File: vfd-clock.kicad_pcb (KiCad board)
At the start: 2 copper layers, 139.7 x 49.5 mm, 24 parts, among them CON1 BARREL_JACK_2, P1 ST_LINK, U1 Maple_Mini_(BTE14-07), U2 CD4056, U3 CD4056, U4 CD4056, U5 CD4056, U6 CD4056, U7 CD4056, U9 MC34063

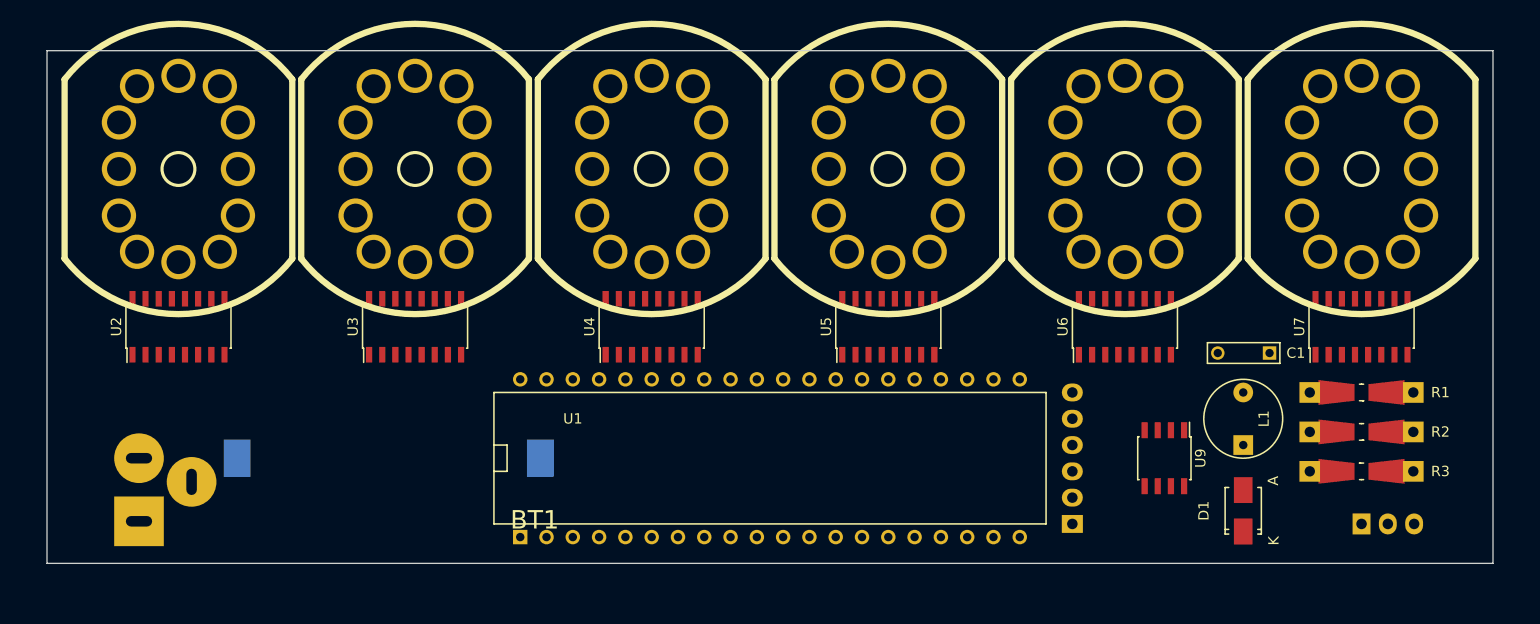
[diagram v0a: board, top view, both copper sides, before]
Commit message: tubes, data bus: routed
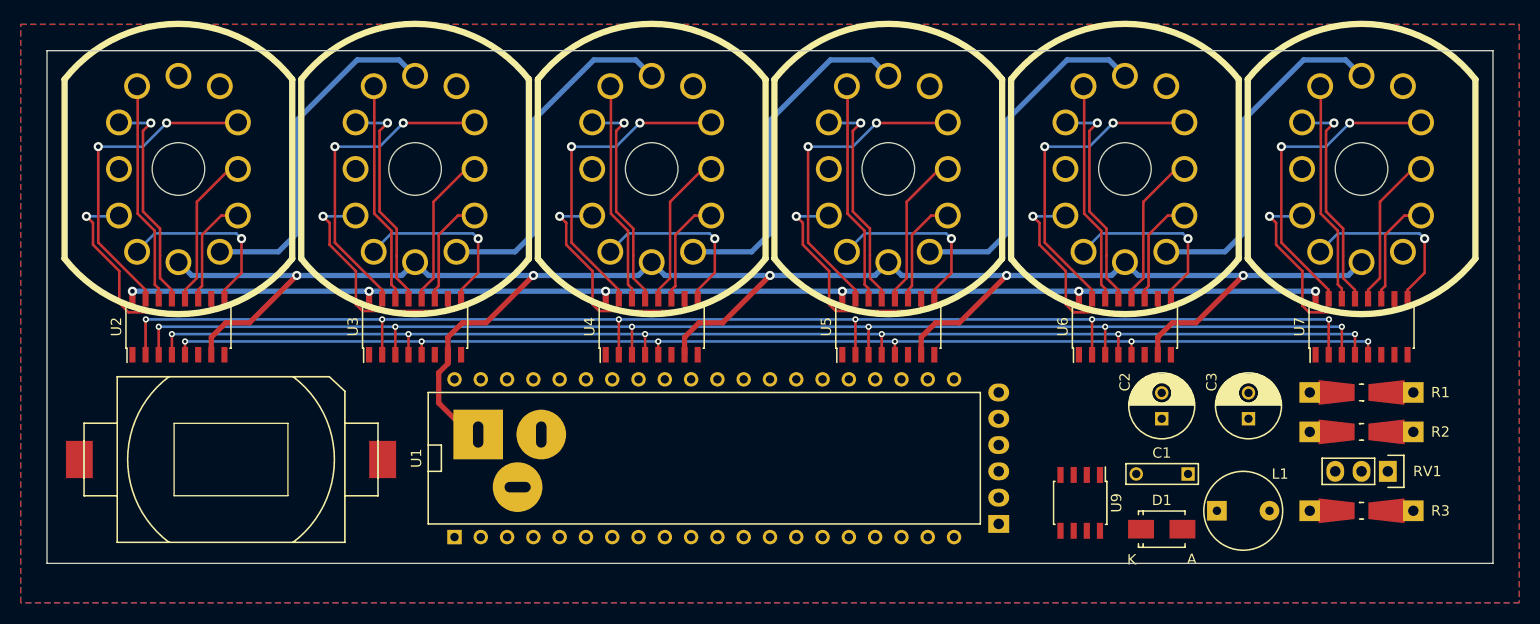
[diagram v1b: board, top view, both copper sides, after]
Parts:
- added C2: 100u, Capacitors_ThroughHole:C_Radial_D6.3_L11.2_P2.5, F.Cu at (122.9, 50.8)
- added C3: 100u, Capacitors_ThroughHole:C_Radial_D6.3_L11.2_P2.5, F.Cu at (131.3, 50.8)
- BT1, RV1: moved to F.Cu
- moved CON1 38.9 mm to (63.0, 52.3), turned to 180 degrees
- moved BT1 15.2 mm to (33.0, 54.7)
- moved C1 14.1 mm to (125.5, 56.1)
- moved U9 9.20 mm to (115.1, 58.9)
- moved L1 8.89 mm to (130.8, 59.7), turned to 0 degrees
- moved D1 8.07 mm to (122.9, 61.5), turned to 0 degrees
- moved P1 7.11 mm to (107.2, 61.0)
- moved U1 6.35 mm to (78.7, 54.6)
- moved RV1 5.68 mm to (144.8, 55.9)
- moved R3 3.81 mm to (142.2, 59.7)
- turned R2 to 0 degrees
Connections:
- net Net-(R1-Pad2) renamed /REG_HI
- V1 pad 12: /7v2 -> /GND
- V1 pad 5: Net-(V1-Pad5) -> /FIL1
- V2 pad 12: Net-(V2-Pad12) -> /FIL1
- V2 pad 5: Net-(V2-Pad5) -> /FIL2
- V3 pad 12: Net-(V3-Pad12) -> /FIL2
- V3 pad 5: Net-(V3-Pad5) -> /FIL3
- V4 pad 12: Net-(V1-Pad5) -> /FIL3
- V4 pad 5: Net-(V2-Pad12) -> /FIL4
- V5 pad 12: Net-(V2-Pad5) -> /FIL4
- V5 pad 5: Net-(V3-Pad12) -> /FIL5
- V6 pad 12: Net-(V3-Pad5) -> /FIL5
- V6 pad 5: /GND -> /7v2
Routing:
- net /19v5: track 0.00 -> 191.9 mm, vias 0 -> 5
- net /DC: track 0.00 -> 134.8 mm, vias 0 -> 6
- net /DB: track 0.00 -> 130.5 mm, vias 0 -> 6
- net /DD: track 0.00 -> 126.2 mm, vias 0 -> 6
- net /DA: track 0.00 -> 122.0 mm, vias 0 -> 6
- net /3v3: track 0.00 -> 118.7 mm, vias 0 -> 6
- net /FIL5: track 0.00 -> 33.6 mm
- net /FIL4: track 0.00 -> 33.6 mm
- net /FIL3: track 0.00 -> 33.6 mm
- net /FIL2: track 0.00 -> 33.6 mm
- net /FIL1: track 0.00 -> 33.6 mm
- net Net-(U6-Pad15): track 0.00 -> 31.1 mm, vias 0 -> 2
- net Net-(U5-Pad15): track 0.00 -> 31.1 mm, vias 0 -> 2
- net Net-(U3-Pad15): track 0.00 -> 31.1 mm, vias 0 -> 2
- net Net-(U7-Pad15): track 0.00 -> 31.1 mm, vias 0 -> 2
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- added copper zone on B.Cu, net /GND
- added copper zone on F.Cu, net /GND
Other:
- net class D_BUS added: clearance 0.254, trace_width 0.254, via_dia 0.6, via_drill 0.3
- net class Power: trace_width 0.381 -> 0.508
- rule via_min_drill: 0.508 -> 0.254
- rule via_min_size: 0.889 -> 0.381

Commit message: first fully routed revision
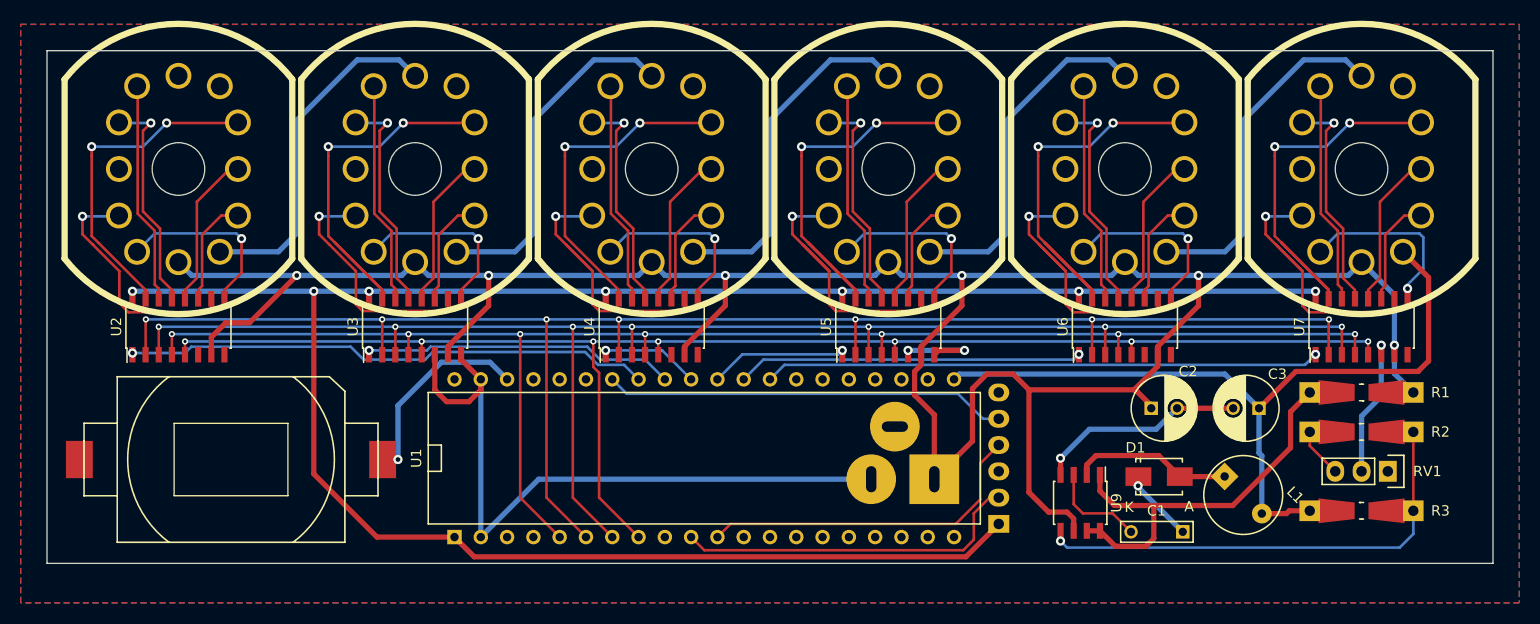
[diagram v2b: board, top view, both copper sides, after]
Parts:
- moved CON1 32.2 mm to (94.9, 56.6), turned to 0 degrees
- moved C1 5.61 mm to (125.0, 61.7)
- moved D1 5.09 mm to (122.7, 56.4)
- moved L1 1.52 mm to (130.8, 58.2), turned to 315 degrees
- moved C2 1.44 mm to (121.9, 49.8), turned to 0 degrees
- moved C3 1.44 mm to (132.3, 49.8), turned to 180 degrees
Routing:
- net /GND: track 0.00 -> 118.5 mm, vias 0 -> 5
- net /3v3: track 118.7 -> 207.1 mm, vias 6 -> 7
- net /7v2: track 0.00 -> 78.5 mm
- net /19v5: track 191.9 -> 250.9 mm, vias 5 -> 6
- net /STROBE6: track 0.00 -> 53.7 mm, vias 0 -> 1
- net /STROBE1: track 0.00 -> 51.2 mm, vias 0 -> 1
- net Net-(R2-Pad2): track 0.00 -> 50.9 mm, vias 0 -> 1
- net /REG_HI: track 0.00 -> 42.1 mm
- net /RST: track 0.00 -> 39.1 mm
- net /SWCLK: track 0.00 -> 33.8 mm
- net /STROBE5: track 0.00 -> 33.4 mm, vias 0 -> 1
- net Net-(U5-Pad15): track 31.1 -> 64.3 mm
- net /SWDIO: track 0.00 -> 32.9 mm
- net /STROBE2: track 0.00 -> 30.5 mm, vias 0 -> 1
- net /DC: track 134.8 -> 157.4 mm, vias 6 -> 7
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
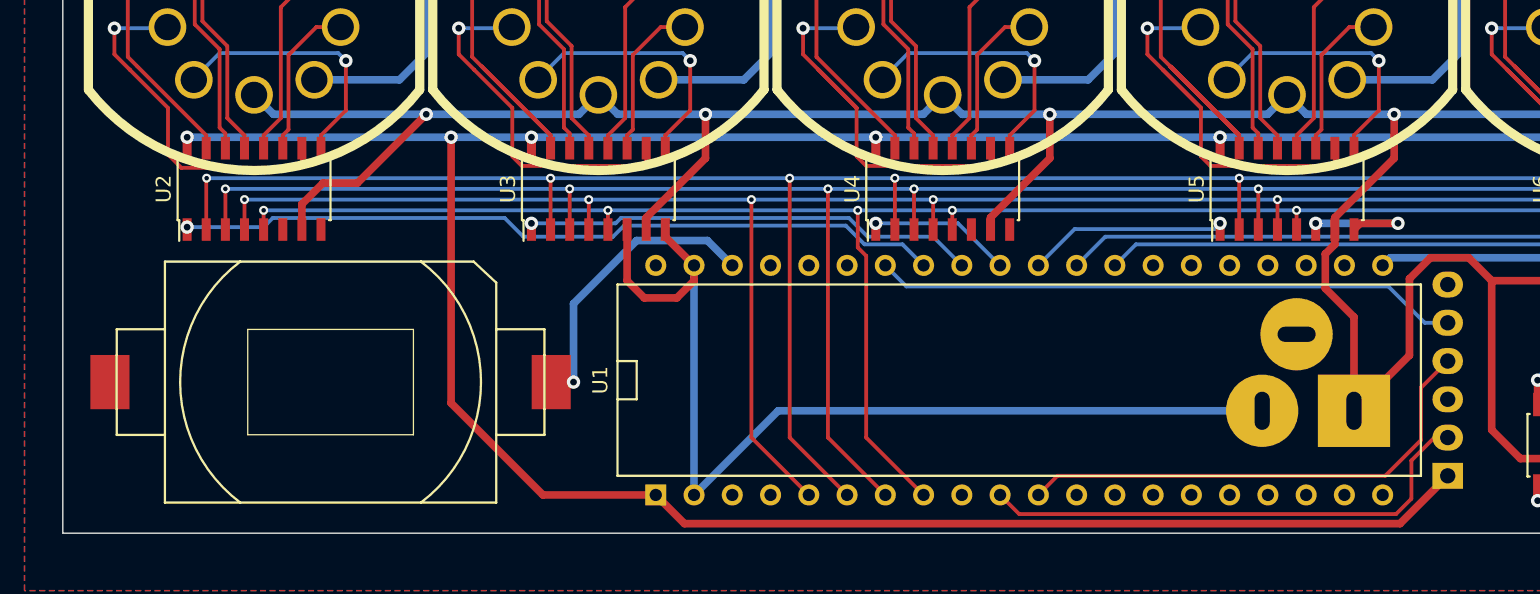
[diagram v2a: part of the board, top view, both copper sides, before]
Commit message: second redundant power connector footprint
(I expect to only ever populate one or the other.)
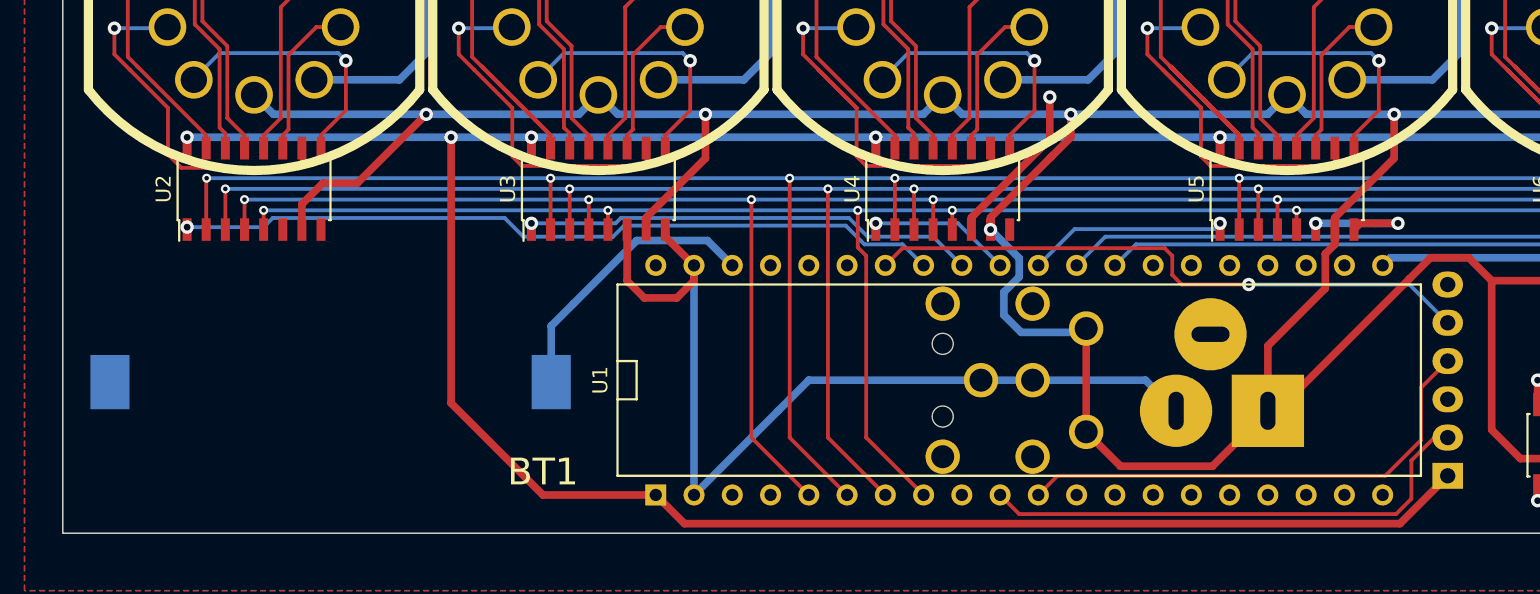
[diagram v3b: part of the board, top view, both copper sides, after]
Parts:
- added CON2: BARREL_JACK_2, VFD:OCT_JACK, B.Cu at (77.0, 54.6)
- BT1: moved to B.Cu
- moved CON1 5.72 mm to (89.2, 56.6)
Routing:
- net /19v5: track 250.9 -> 289.5 mm, vias 6 -> 7
- net /GND: track 118.5 -> 125.5 mm, vias 5 -> 6
- net /RST: track 39.1 -> 40.6 mm, vias 0 -> 1
- net /Vbat: track 19.6 -> 18.8 mm, vias 1 -> 0

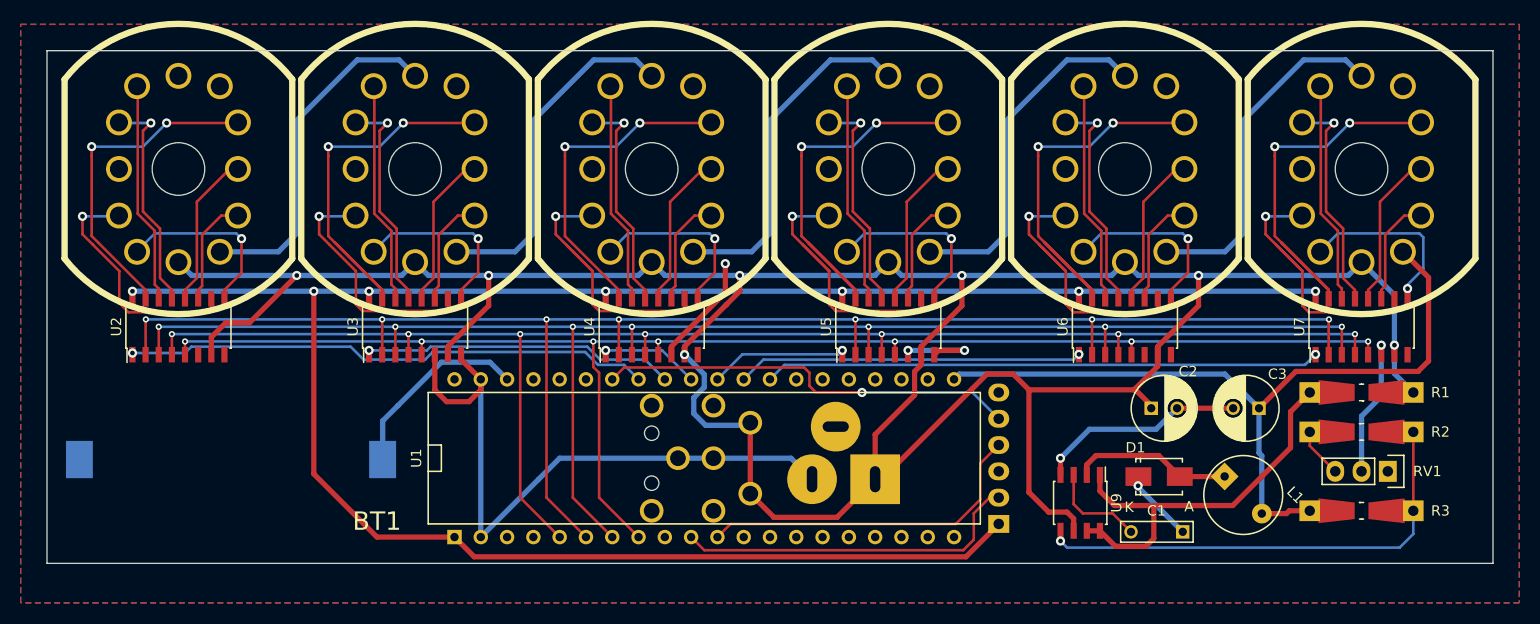
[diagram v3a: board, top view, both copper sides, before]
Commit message: add buttons to set time
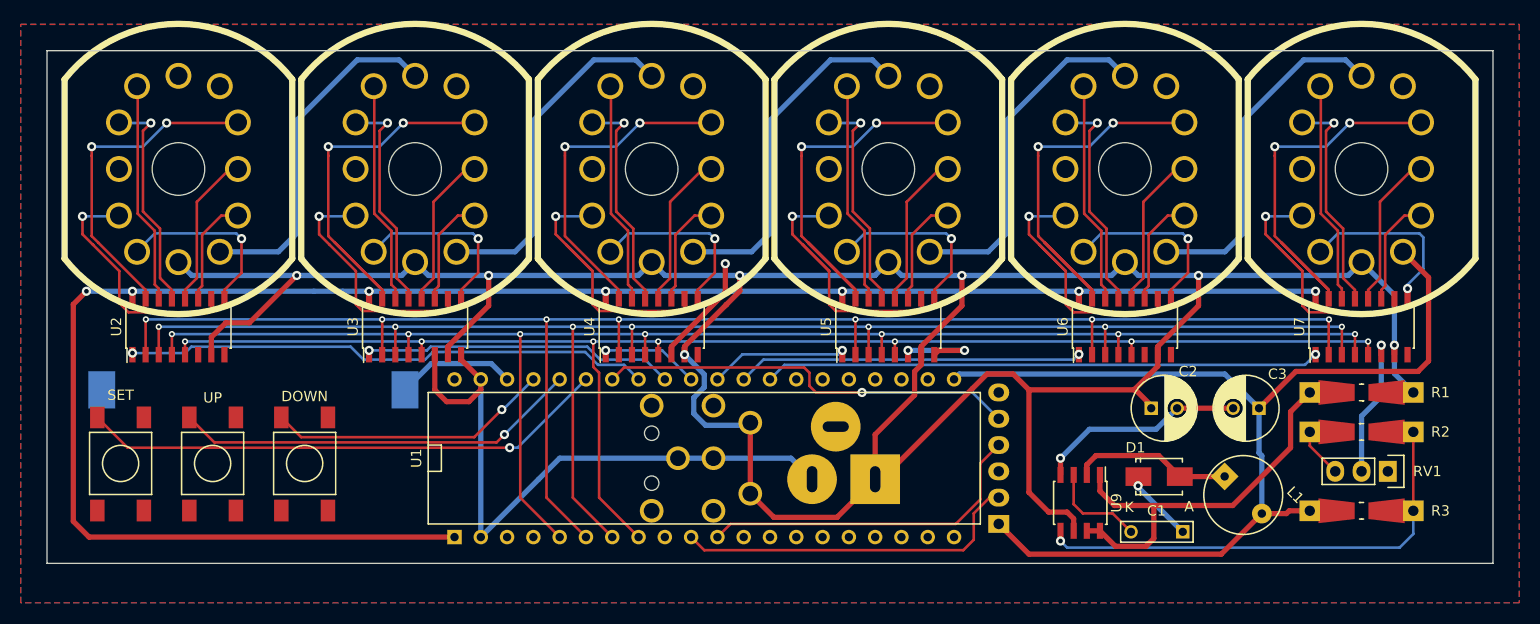
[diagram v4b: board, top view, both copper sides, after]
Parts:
- added REF**: Symbol_OSHW-Logo_SilkScreen, Symbols:Symbol_OSHW-Logo_SilkScreen, B.Cu at (130.8, 18.9)
- added SW1: SET, VFD:SMD_TACT_6mm, F.Cu at (22.4, 55.1)
- added SW2: UP, VFD:SMD_TACT_6mm, F.Cu at (31.2, 55.1)
- added SW3: DOWN, VFD:SMD_TACT_6mm, F.Cu at (40.1, 55.1)
- moved BT1 7.07 mm to (35.2, 48.0)
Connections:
- P1 pad 1: /3v3 -> /7v2
- U1 pad 35: (no net) -> /BTN_SET
- U1 pad 36: (no net) -> /BTN_UP
- U1 pad 37: (no net) -> /BTN_DN
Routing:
- net /BTN_SET: track 0.00 -> 51.2 mm, vias 0 -> 1
- net /BTN_UP: track 0.00 -> 39.3 mm, vias 0 -> 1
- net /7v2: track 78.5 -> 106.8 mm
- net /BTN_DN: track 0.00 -> 27.5 mm, vias 0 -> 1
- net /3v3: track 207.1 -> 183.3 mm
- net /Vbat: track 18.8 -> 11.5 mm
